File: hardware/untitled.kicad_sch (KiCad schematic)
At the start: 38 parts, among them IC1 ESP32-S3-WROOM-1-N8R8, J5 DCJ200-10-A-K1-K, J6 USB4105-GF-A, SW1 SW_Push, SW2 SW_Push, U3 NCP1117ST33T3G, U4 USBLC6-2SC6

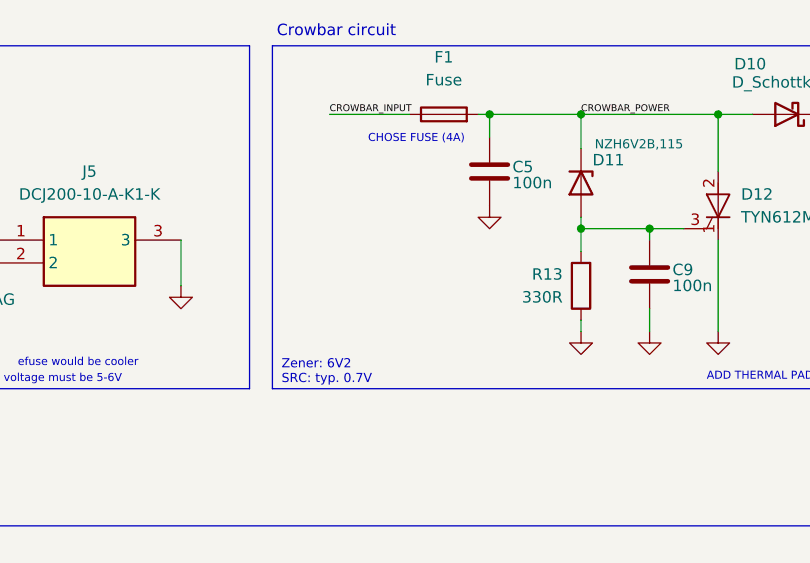
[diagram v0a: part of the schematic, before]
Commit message: Schematics adjustments - updated some components
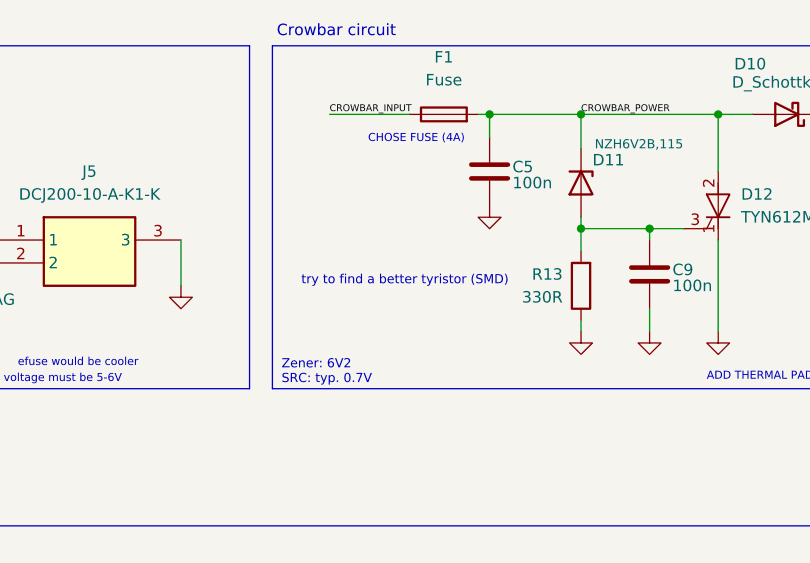
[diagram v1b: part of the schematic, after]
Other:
- note added: "try to find a better tyristor (SMD)"
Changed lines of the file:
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@@
+		)
+	)
+	(text "try to find a better tyristor (SMD)"
+		(exclude_from_sim no)
+		(at 217.932 46.482 0)
+		(effects
+			(font
+				(size 1.016 1.016)
+				(color 255 0 0 1)
+			)
 		)
 	)

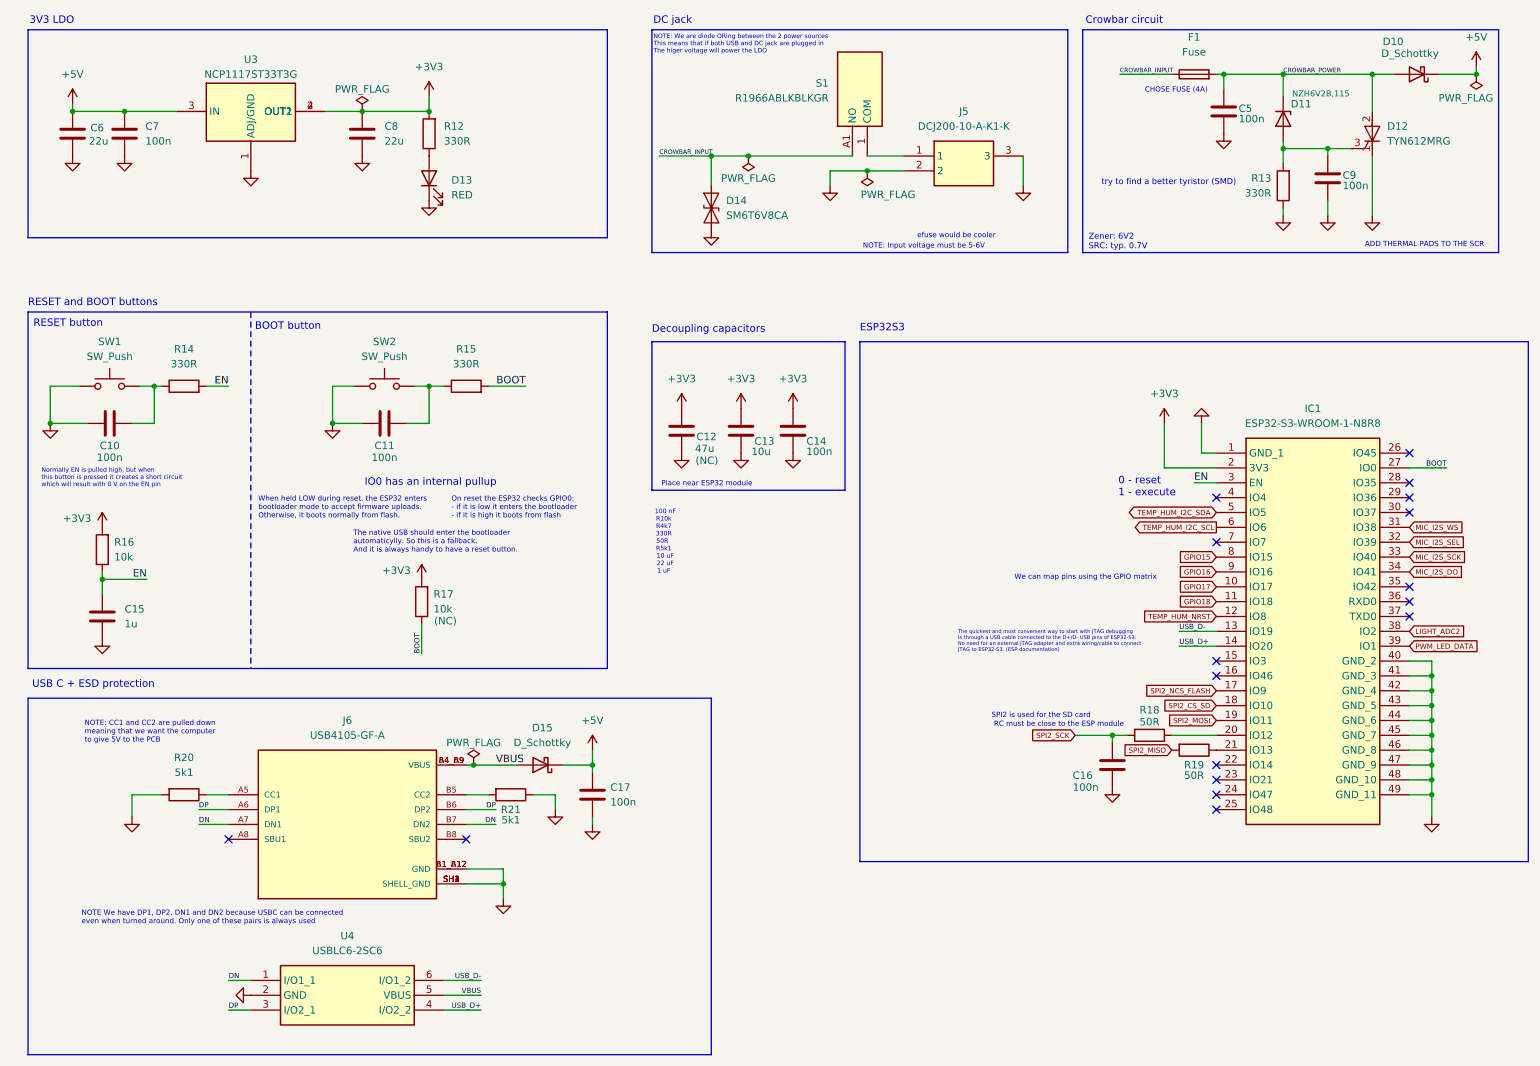
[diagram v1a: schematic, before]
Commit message: Added notes to schematics, SPI modifications
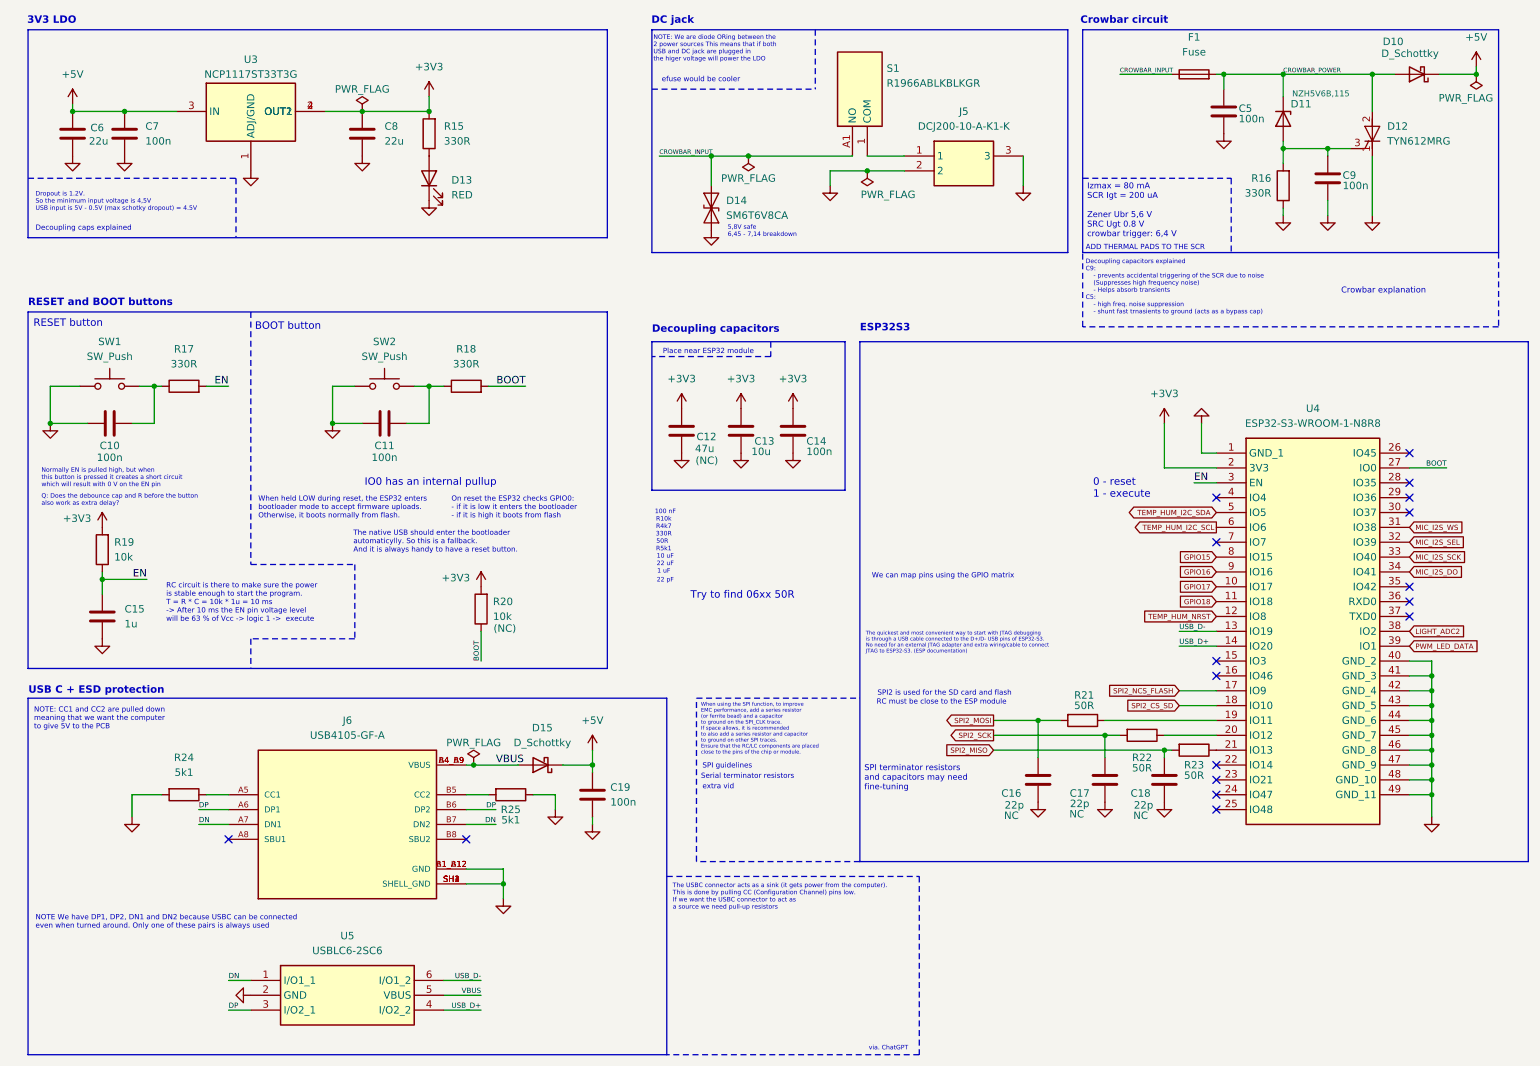
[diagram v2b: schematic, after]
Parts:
- added C16, C18: 22p, Capacitor_SMD:C_0805_2012Metric_Pad1.18x1.45mm_HandSolder, symbol Device:C
- added R21: 50R, Resistor_SMD:R_0402_1005Metric_Pad0.72x0.64mm_HandSolder, symbol Device:R
- C17: renamed from C16; value 100n -> 22p; Note (none) -> NC
- D11: value NZH6V2B,115 -> NZH5V6B,115
- D12: footprint ESP32-project-footprints:TO255P460X1020X2005-3P -> ESP32-project-footprints:TS820600B
- renumbered C17 to C19, R12 to R15, R13 to R16, R14 to R17, R15 to R18, R16 to R19, R17 to R20, R18 to R22, R19 to R23, R20 to R24, R21 to R25, IC1 to U4, U4 to U5
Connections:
- net GND: now also C16.1, C18.1
- net SPI2_MISO: now also C18.2
- net SPI2_MOSI: now also C16.2, R21.2; no longer U4.19 (IO11)
- new net: R21.1, U4.19 (IO11)
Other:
- note added: "22 pF"
- note added: "5,8V safe 6,45 - 7,14 breakdown"
- note added: "Crowbar explanation"
- note added: "Decoupling capacitors explained C9: - prevents accidental triggering of the SCR due to noise (Suppresses high frequency noise) - Helps absorb transients C5: - high freq. noise suppression - shunt fast trnasients to ground (acts as a bypass cap)"
- note added: "Decoupling caps explained"
- note added: "Dropout is 1.2V. So the minimum input voltage is 4,5V USB input is 5V - 0.5V (max schotky dropout) = 4.5V"
- note added: "Izmax = 80 mA SCR Igt = 200 uA Zener Ubr 5,6 V SRC Ugt 0.8 V crowbar trigger: 6,4 V"
- note added: "NOTE: We are diode ORing between the 2 power sources This means that if both USB and DC jack are plugged in the higer voltage will power the LDO"
- note added: "Q: Does the debounce cap and R before the button also work as extra delay?"
- note added: "RC circuit is there to make sure the power is stable enough to start the program. T = R * C = 10k * 1u = 10 ms -> After 10 ms the EN pin voltage level will be 63 % of Vcc -> logic 1 -> execute"
- note added: "SPI guidelines"
- note added: "SPI terminator resistors and capacitors may need fine-tuning"
- note added: "SPI2 is used for the SD card and flash"
- note added: "Serial terminator resistors"
- note added: "The USBC connector acts as a sink (it gets power from the computer). This is done by pulling CC (Configuration Channel) pins low. If we want the USBC connector to act as a source we need pull-up resistors"
- note added: "Try to find 06xx 50R"
- note added: "When using the SPI function, to improve EMC performance, add a series resistor (or ferrite bead) and a capacitor to ground on the SPI_CLK trace. If space allows, it is recommended to also add a series resistor and capacitor to ground on other SPI traces. Ensure that the RC/LC components are placed close to the pins of the chip or module."
- note added: "extra vid"
- note added: "via. ChatGPT"
- note removed: "CHOSE FUSE (4A)"
- note removed: "NOTE: Input voltage must be 5-6V"
- note removed: "NOTE: We are diode ORing between the 2 power sources This means that if both USB and DC jack are plugged in The higer voltage will power the LDO"
- note removed: "SPI2 is used for the SD card"
- note removed: "Zener: 6V2 SRC: typ. 0.7V"
- note removed: "try to find a better tyristor (SMD)"
- moved on the sheet: C17, R20, R22

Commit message: Layout v0,4
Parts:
- R21, R22, R23: footprint Resistor_SMD:R_0402_1005Metric_Pad0.72x0.64mm_HandSolder -> Resistor_SMD:R_0603_1608Metric_Pad0.98x0.95mm_HandSolder
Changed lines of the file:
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@@
 			)
 		)
-		(property "Footprint" "Resistor_SMD:R_0402_1005Metric_Pad0.72x0.64mm_HandSolder"
+		(property "Footprint" "Resistor_SMD:R_0603_1608Metric_Pad0.98x0.95mm_HandSolder"
 			(at 222.25 141.732 90)
 			(effects
@@
 			)
 		)
-		(property "Footprint" "Resistor_SMD:R_0402_1005Metric_Pad0.72x0.64mm_HandSolder"
+		(property "Footprint" "Resistor_SMD:R_0603_1608Metric_Pad0.98x0.95mm_HandSolder"
 			(at 213.36 139.192 90)
 			(effects
@@
 			)
 		)
-		(property "Footprint" "Resistor_SMD:R_0402_1005Metric_Pad0.72x0.64mm_HandSolder"
+		(property "Footprint" "Resistor_SMD:R_0603_1608Metric_Pad0.98x0.95mm_HandSolder"
 			(at 203.2 136.652 90)
 			(effects
